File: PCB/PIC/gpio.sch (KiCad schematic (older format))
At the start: 16 parts, among them P13 I2C, P14 SPI, P16 ZX62-B-5PA, P5 CONN_13X2, P6 CONN_5X2

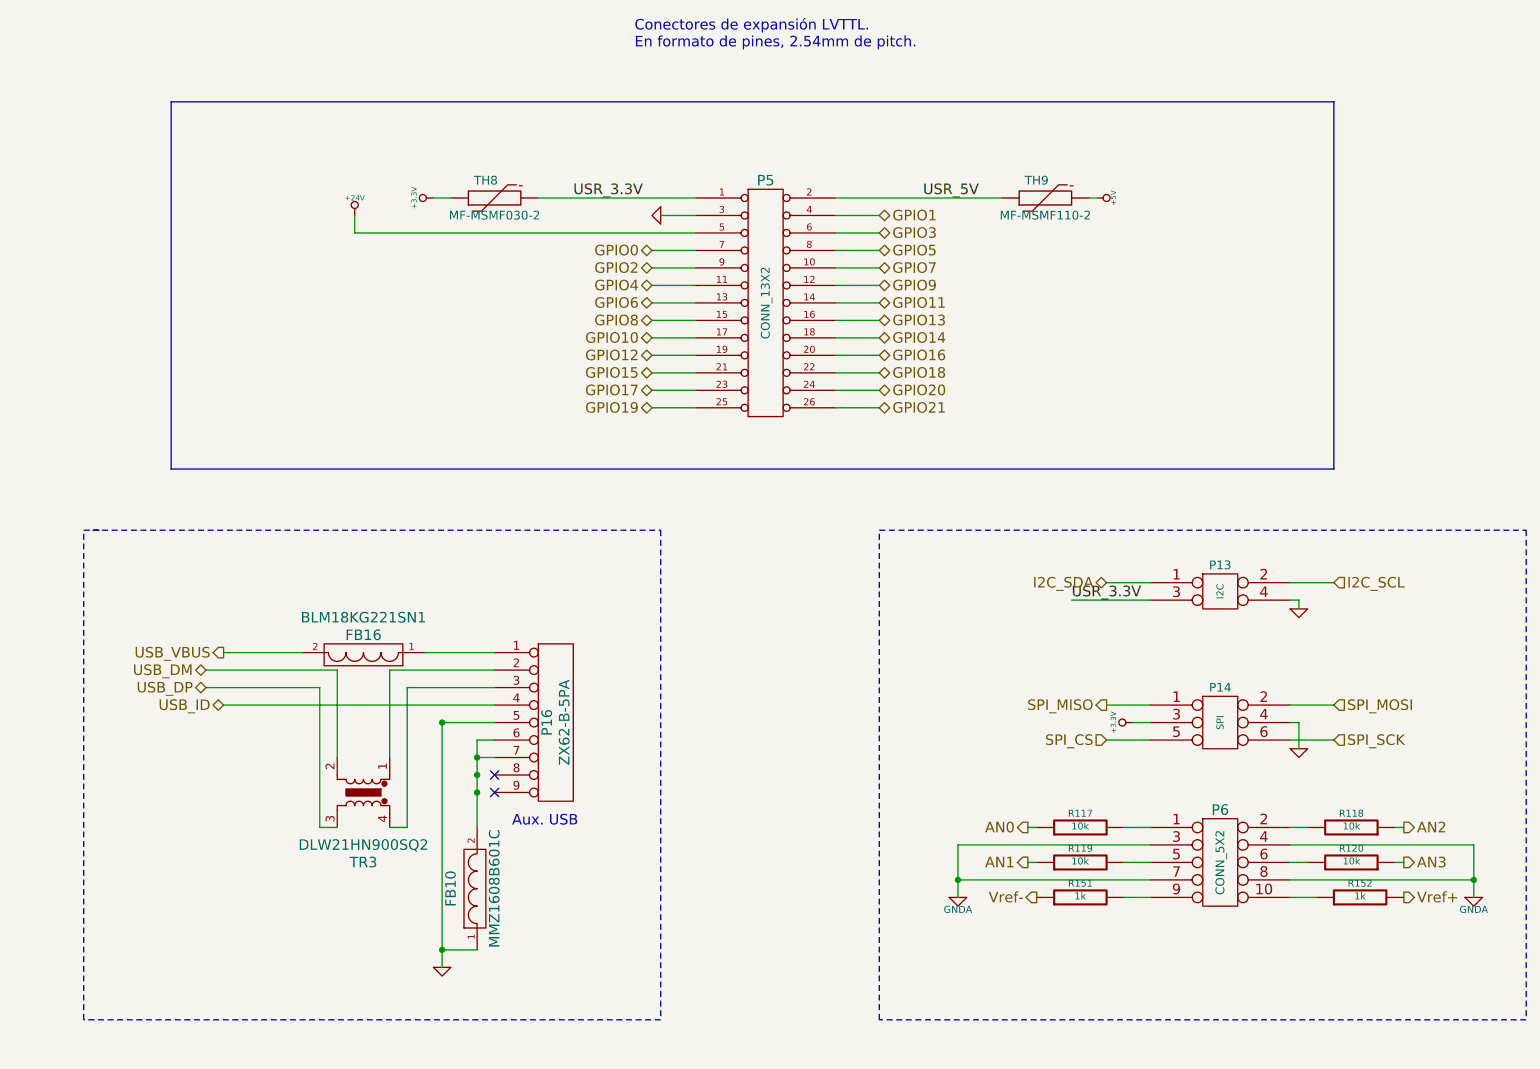
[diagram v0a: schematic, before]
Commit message: CIAA PIC correccion FT232RL
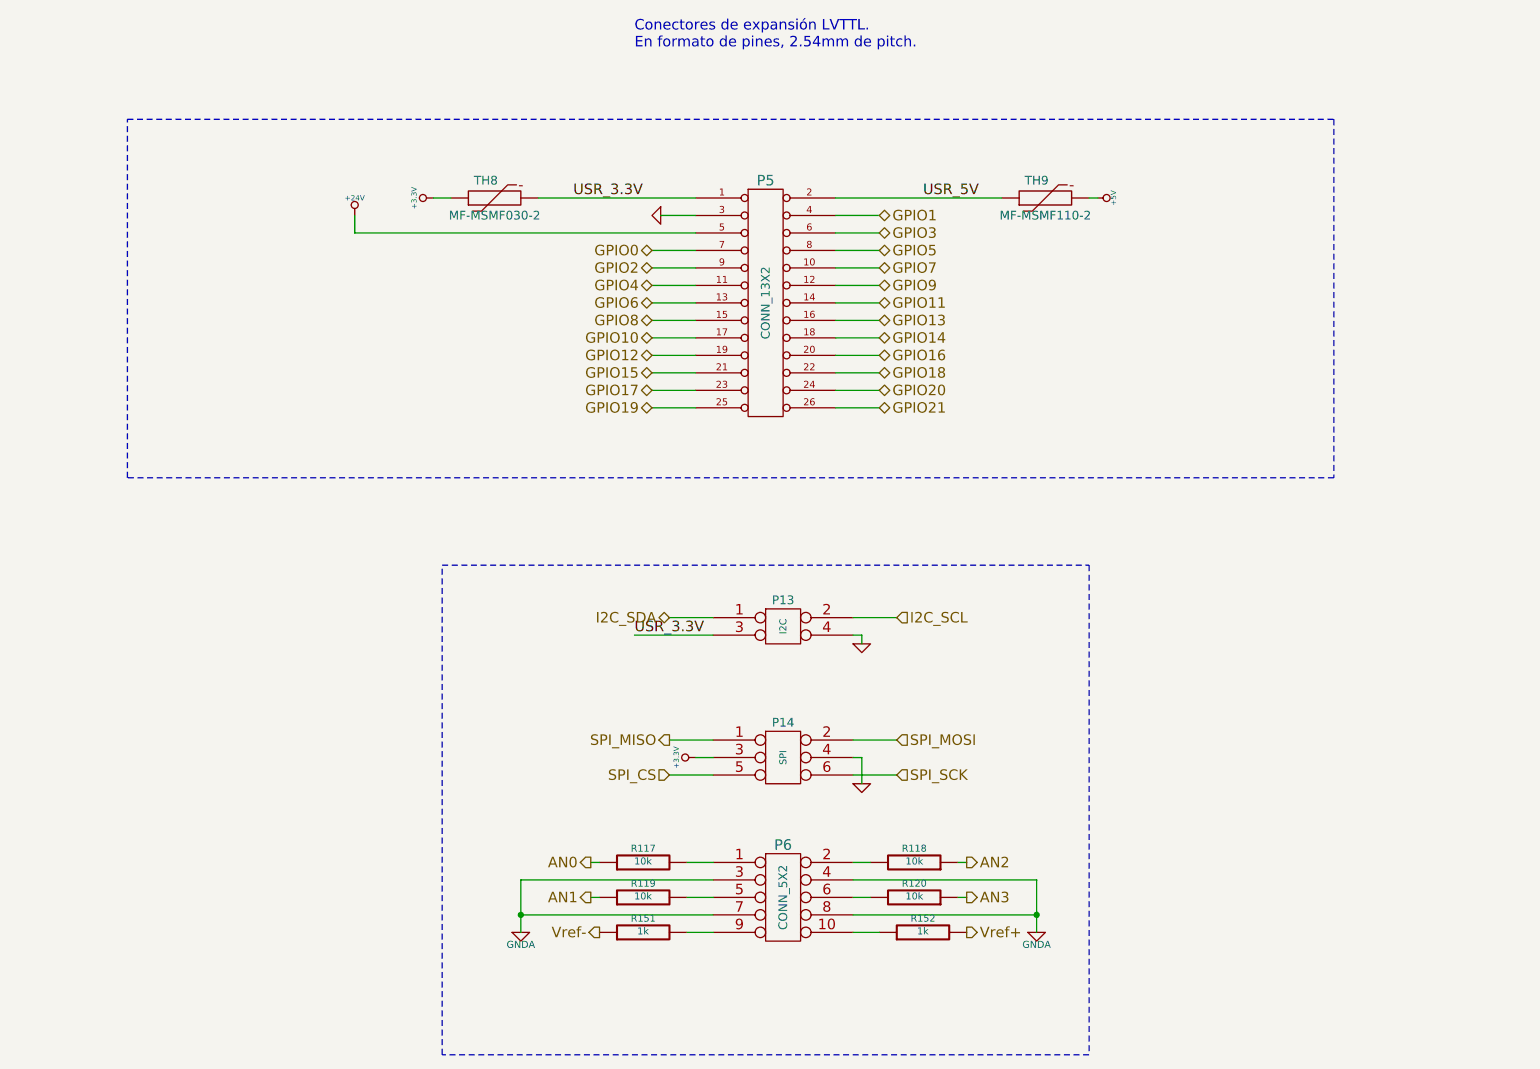
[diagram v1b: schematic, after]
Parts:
- removed FB10: MMZ1608B601C, ~, symbol FILTER
- removed FB16: BLM18KG221SN1, ~, symbol FILTER
- removed P16: ZX62-B-5PA, symbol CONN_9
- removed TR3: DLW21HN900SQ2, symbol TRASF_UNIP
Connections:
- no-connect marks 2 -> 0
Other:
- note removed: "Aux. USB"
- moved on the sheet: P13, P14, P6, R117, R118, R119, R120, R151, R152

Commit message: CIAA PIC footprints done
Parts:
- added R166, R167, R168, R169, R170, R171, R172, R173, R174, R175, R176, R177, R178, R179, R180, R181, R182, R183, R184, R185, R186, R187: 10k, ~, symbol R
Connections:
- net GND: now also R166.1, R167.1, R168.1, R169.1, R170.1, R171.1, R172.1, R173.1, R174.1, R175.1, R176.2, R177.2, R178.2, R179.2, R180.2, R181.2, R182.2, R183.2, R184.2, R185.2, R186.2, R187.2
- net GPIO0: now also R166.2
- net GPIO1: now also R176.1
- net GPIO10: now also R171.2
- net GPIO11: now also R181.1
- net GPIO12: now also R172.2; no longer P5.19 (P19)
- net GPIO13: now also R182.1
- net GPIO14: now also R183.1
- net GPIO15: now also R173.2
- net GPIO16: now also R184.1
- net GPIO17: now also R174.2
- net GPIO18: now also R185.1
- net GPIO19: now also R175.2
- net GPIO2: now also R167.2
- net GPIO20: now also R186.1
- net GPIO21: now also R187.1
- net GPIO3: now also R177.1
- net GPIO4: now also R168.2
- net GPIO5: now also R178.1
- net GPIO6: now also R169.2
- net GPIO7: now also R179.1
- net GPIO8: now also R170.2
- net GPIO9: now also R180.1
- no-connect marks 0 -> 1

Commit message: Correcciones al esquematico segun rev01
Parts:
- removed P13: I2C, symbol CONN_2X2
- removed P5: CONN_13X2, symbol CONN_13X2
- removed P6: CONN_5X2, symbol CONN_5X2
- removed R151, R152: 1k, ~, symbol R
- removed R166, R167, R168, R169, R170, R171, R172, R173, R174, R175, R176, R177, R178, R179, R180, R181, R182, R183, R184, R185, R186, R187: 10k, ~, symbol R
- added P1: CONN_6X2, symbol CONN_6X2
- added P6: CONN_4X2, symbol CONN_4X2
- R117, R118, R119, R120: symbol R -> R-RESCUE-ciaa-pic
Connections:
- net GND: now also P1.3 (P3)
- net GNDA: now also P6.3, P6.4, P6.7, P6.8
- net GPIO0: now also P1.6 (P6)
- net GPIO13: now also P1.2 (P2)
- net GPIO15: now also P1.1 (P1)
- net GPIO2: now also P1.7 (P7)
- net GPIO3: now also P1.4 (P4)
- net GPIO4: now also P1.9
- net GPIO5: now also P1.8 (P8)
- net GPIO7: now also P1.5 (P5)
- net GPIO8: now also P1.10
- net USR_3.3V: now also P1.11
- net USR_5V: now also P1.12
- net at R117.2: now also P6.1
- net at R119.2: now also P6.5
- net at R118.2: now also P6.2
- net at R120.2: now also P6.6
- no-connect marks 1 -> 0
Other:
- moved on the sheet: P14, R117, R118, R119, R120, TH8, TH9

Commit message: elimino conector salida reles
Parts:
- R117, R118, R119, R120: footprint ~ -> Resistors_SMD:R_0603
- TH8, TH9: footprint ~ -> (none)
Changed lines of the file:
@@
 F 0 "TH8" V 4450 2500 50  0000 C CNN
 F 1 "MF-MSMF030-2" V 4250 2450 50  0000 C CNN
-F 2 "~" H 4350 2450 60  0000 C CNN
+F 2 "" H 4350 2450 60  0001 C CNN
 F 3 "~" H 4350 2450 60  0000 C CNN
 	1    4350 2450
@@
 USR_3.3V
 $Comp
-L +3.3V-RESCUE-ciaa-pic #PWR0233
+L +3.3V-RESCUE-ciaa-pic #PWR0232
 U 1 1 52CA1E6C
 P 4000 2450
-F 0 "#PWR0233" H 4000 2410 30  0001 C CNN
+F 0 "#PWR0232" H 4000 2410 30  0001 C CNN
 F 1 "+3.3V" H 4000 2560 30  0000 C CNN
 F 2 "" H 4000 2450 60  0000 C CNN
@@
 F 0 "TH9" V 7600 2500 50  0000 C CNN
 F 1 "MF-MSMF110-2" V 7400 2450 50  0000 C CNN
-F 2 "~" H 7500 2450 60  0000 C CNN
+F 2 "" H 7500 2450 60  0001 C CNN
 F 3 "~" H 7500 2450 60  0000 C CNN
 	1    7500 2450
@@
 $EndComp
 $Comp
-L GND-RESCUE-ciaa-pic #PWR0234
+L GND-RESCUE-ciaa-pic #PWR0233
 U 1 1 52CA1EC3
 P 5300 2050
-F 0 "#PWR0234" H 5300 2050 30  0001 C CNN
+F 0 "#PWR0233" H 5300 2050 30  0001 C CNN
 F 1 "GND" H 5300 1980 30  0001 C CNN
 F 2 "" H 5300 2050 60  0000 C CNN
@@
 F 0 "R117" V 5280 5000 40  0000 C CNN
 F 1 "10k" V 5207 5001 40  0000 C CNN
-F 2 "~" V 5130 5000 30  0000 C CNN
+F 2 "Resistors_SMD:R_0603" V 5130 5000 30  0001 C CNN
 F 3 "~" H 5200 5000 30  0000 C CNN
 	1    5200 5000
@@
 F 0 "R119" V 5280 5200 40  0000 C CNN
 F 1 "10k" V 5207 5201 40  0000 C CNN
-F 2 "~" V 5130 5200 30  0000 C CNN
+F 2 "Resistors_SMD:R_0603" V 5130 5200 30  0001 C CNN
 F 3 "~" H 5200 5200 30  0000 C CNN
 	1    5200 5200
@@
 F 0 "R118" V 6830 5000 40  0000 C CNN
 F 1 "10k" V 6757 5001 40  0000 C CNN
-F 2 "~" V 6680 5000 30  0000 C CNN
+F 2 "Resistors_SMD:R_0603" V 6680 5000 30  0001 C CNN
 F 3 "~" H 6750 5000 30  0000 C CNN
 	1    6750 5000
@@
 F 0 "R120" V 6830 5200 40  0000 C CNN
 F 1 "10k" V 6757 5201 40  0000 C CNN
-F 2 "~" V 6680 5200 30  0000 C CNN
+F 2 "Resistors_SMD:R_0603" V 6680 5200 30  0001 C CNN
 F 3 "~" H 6750 5200 30  0000 C CNN
 	1    6750 5200
@@
 $EndComp
 $Comp
-L +5V #PWR0235
+L +5V #PWR0234
 U 1 1 52CA305A
 P 7800 2450
-F 0 "#PWR0235" H 7800 2540 20  0001 C CNN
+F 0 "#PWR0234" H 7800 2540 20  0001 C CNN
 F 1 "+5V" H 7800 2540 30  0000 C CNN
 F 2 "" H 7800 2450 60  0000 C CNN
@@
 F 0 "P14" H 6000 4700 50  0000 C CNN
 F 1 "SPI" V 6000 4500 40  0000 C CNN
-F 2 "" H 6000 4450 60  0000 C CNN
+F 2 "" H 6000 4450 60  0001 C CNN
 F 3 "" H 6000 4450 60  0000 C CNN
 	1    6000 4450
@@
 $EndComp
 $Comp
-L GND-RESCUE-ciaa-pic #PWR0236
+L GND-RESCUE-ciaa-pic #PWR0235
 U 1 1 52CCD441
 P 6450 4550
-F 0 "#PWR0236" H 6450 4550 30  0001 C CNN
+F 0 "#PWR0235" H 6450 4550 30  0001 C CNN
 F 1 "GND" H 6450 4480 30  0001 C CNN
 F 2 "" H 6450 4550 60  0000 C CNN
@@
 Conectores de expansión LVTTL.\nEn formato de pines, 2.54mm de pitch.
 $Comp
-L GNDA-RESCUE-ciaa-pic #PWR0237
+L GNDA-RESCUE-ciaa-pic #PWR0236
 U 1 1 52DEB0C3
 P 7450 5400
-F 0 "#PWR0237" H 7450 5400 40  0001 C CNN
+F 0 "#PWR0236" H 7450 5400 40  0001 C CNN
 F 1 "GNDA" H 7450 5330 40  0000 C CNN
 F 2 "" H 7450 5400 60  0000 C CNN
@@
 $EndComp
 $Comp
-L GNDA-RESCUE-ciaa-pic #PWR0238
+L GNDA-RESCUE-ciaa-pic #PWR0237
 U 1 1 52DEB0D0
 P 4500 5400
-F 0 "#PWR0238" H 4500 5400 40  0001 C CNN
+F 0 "#PWR0237" H 4500 5400 40  0001 C CNN
 F 1 "GNDA" H 4500 5330 40  0000 C CNN
 F 2 "" H 4500 5400 60  0000 C CNN
@@
 $EndComp
 $Comp
-L +3.3V-RESCUE-ciaa-pic #PWR0239
+L +3.3V-RESCUE-ciaa-pic #PWR0238
 U 1 1 5344A9C9
 P 5500 4400
-F 0 "#PWR0239" H 5500 4360 30  0001 C CNN
+F 0 "#PWR0238" H 5500 4360 30  0001 C CNN
 F 1 "+3.3V" H 5500 4510 30  0000 C CNN
 F 2 "" H 5500 4400 60  0000 C CNN
@@
 F 0 "P1" H 5900 2550 60  0000 C CNN
 F 1 "CONN_6X2" V 5900 2200 60  0000 C CNN
-F 2 "" H 5900 2200 60  0000 C CNN
+F 2 "" H 5900 2200 60  0001 C CNN
 F 3 "" H 5900 2200 60  0000 C CNN
 	1    5900 2200
@@
 F 0 "P6" H 6000 5400 50  0000 C CNN
 F 1 "CONN_4X2" V 6000 5150 40  0000 C CNN
-F 2 "" H 6000 5150 60  0000 C CNN
+F 2 "" H 6000 5150 60  0001 C CNN
 F 3 "" H 6000 5150 60  0000 C CNN
 	1    6000 5150

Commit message: rev02 aignacion footprint
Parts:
- P1: footprint (none) -> footprints:PIN_ARRAY_6X2
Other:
- note added: "GPIO"
- note added: "SPI - ADC"
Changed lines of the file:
@@
 	1    0    0    -1
 $EndComp
-Text Notes 5150 900  0    60   ~ 0
+Text Notes 5150 900  0    60   ~ 12
 Conectores de expansión LVTTL.\nEn formato de pines, 2.54mm de pitch.
 $Comp
@@
 F 0 "P1" H 5900 2550 60  0000 C CNN
 F 1 "CONN_6X2" V 5900 2200 60  0000 C CNN
-F 2 "" H 5900 2200 60  0001 C CNN
+F 2 "footprints:PIN_ARRAY_6X2" H 5900 2200 60  0001 C CNN
 F 3 "" H 5900 2200 60  0000 C CNN
 	1    5900 2200
@@
 	1    0    0    -1
 $EndComp
+Text Notes 9300 1300 0    99   ~ 20
+GPIO
+Text Notes 6900 3500 0    99   ~ 20
+SPI - ADC
 $EndSCHEMATC

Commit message: rev.02 CIAA-PIC
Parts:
- R117, R118, R119, R120: #Digikey (none) -> 311-10KGRCT-ND; #manf (none) -> RC0603JR-0710KL
- TH8: #Digikey (none) -> MF-MSMF030-2CT-ND; #manf (none) -> MF-MSMF030-2
- TH9: #Digikey (none) -> MF-MSMF110-2CT-ND; #manf (none) -> MF-MSMF110-2
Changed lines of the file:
@@
 F 2 "" H 4350 2450 60  0001 C CNN
 F 3 "~" H 4350 2450 60  0000 C CNN
+F 4 "MF-MSMF030-2CT-ND " V 4350 2450 60  0001 C CNN "#Digikey"
+F 5 "MF-MSMF030-2 " V 4350 2450 60  0001 C CNN "#manf"
 	1    4350 2450
 	0    -1   -1   0
@@
 F 2 "" H 7500 2450 60  0001 C CNN
 F 3 "~" H 7500 2450 60  0000 C CNN
+F 4 " MF-MSMF110-2CT-ND" V 7500 2450 60  0001 C CNN "#Digikey"
+F 5 "MF-MSMF110-2 " V 7500 2450 60  0001 C CNN "#manf"
 	1    7500 2450
 	0    -1   -1   0
@@
 F 2 "Resistors_SMD:R_0603" V 5130 5000 30  0001 C CNN
 F 3 "~" H 5200 5000 30  0000 C CNN
+F 4 "311-10KGRCT-ND " V 5200 5000 60  0001 C CNN "#Digikey"
+F 5 "RC0603JR-0710KL" V 5200 5000 60  0001 C CNN "#manf"
 	1    5200 5000
 	0    -1   -1   0
@@
 F 2 "Resistors_SMD:R_0603" V 5130 5200 30  0001 C CNN
 F 3 "~" H 5200 5200 30  0000 C CNN
+F 4 "311-10KGRCT-ND " V 5200 5200 60  0001 C CNN "#Digikey"
+F 5 "RC0603JR-0710KL" V 5200 5200 60  0001 C CNN "#manf"
 	1    5200 5200
 	0    -1   -1   0
@@
 F 2 "Resistors_SMD:R_0603" V 6680 5000 30  0001 C CNN
 F 3 "~" H 6750 5000 30  0000 C CNN
+F 4 "311-10KGRCT-ND " V 6750 5000 60  0001 C CNN "#Digikey"
+F 5 "RC0603JR-0710KL" V 6750 5000 60  0001 C CNN "#manf"
 	1    6750 5000
 	0    1    -1   0
@@
 F 2 "Resistors_SMD:R_0603" V 6680 5200 30  0001 C CNN
 F 3 "~" H 6750 5200 30  0000 C CNN
+F 4 "311-10KGRCT-ND " V 6750 5200 60  0001 C CNN "#Digikey"
+F 5 "RC0603JR-0710KL" V 6750 5200 60  0001 C CNN "#manf"
 	1    6750 5200
 	0    1    -1   0
